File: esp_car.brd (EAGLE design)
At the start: 81.6 x 84 mm, 50 parts, among them IC1 TB6612FNG, IC2 LT1963ES8-3.3, SW2 SK-12D01, U1 ESP-WROOM-32_NOFLASH

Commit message: art work
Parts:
- removed IC1: TB6612FNG, adafruit:SSOP24
- added U$1: TB6612_NEW, adafruit_my:SSOP24_TB6612
- moved T0 49.4 mm to (76.8, 53.4)
- moved T2 42.5 mm to (57.1, 39.4)
- moved T1 36.7 mm to (68.2, 39.4)
- moved T3 33.0 mm to (47.8, 39.5)
- moved T5 32.1 mm to (18.0, 39.4)
- moved SJ1 2.80 mm to (36.6, 29.8), turned to 180 degrees
- moved C9 2.24 mm to (40.0, 70.0)
- moved SW2 2.00 mm to (40.0, 2.70)
- moved R2 1.03 mm to (38.1, 67.0)
- turned C10 to 180 degrees
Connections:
- net +3V3: now also U$1.20; no longer IC1.20
- net GND: now also U$1.0304, U$1.0910, U$1.18; no longer IC1.10, IC1.18, IC1.3, IC1.4, IC1.9
- net ML+: now also U$1.0102; no longer IC1.1, IC1.2
- net ML-: now also U$1.0506; no longer IC1.5, IC1.6
- net ML_IN1: now also U$1.21; no longer IC1.21
- net ML_IN2: now also U$1.22; no longer IC1.22
- net ML_PWM: now also U$1.23; no longer IC1.23
- net MR+: now also U$1.1112; no longer IC1.11, IC1.12
- net MR-: now also U$1.0708; no longer IC1.7, IC1.8
- net MR_IN1: now also U$1.17; no longer IC1.17
- net MR_IN2: now also U$1.16; no longer IC1.16
- net MR_PWM: now also U$1.15; no longer IC1.15
- net N$7: now also U$1.19; no longer IC1.19
- net VDD: now also U$1.1314, U$1.24; no longer IC1.13, IC1.14, IC1.24
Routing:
- net GND: track 0.00 -> 373.9 mm, vias 0 -> 12
- net +3V3: track 0.00 -> 226.4 mm, vias 0 -> 7
- net +5V: track 0.00 -> 196.2 mm, vias 0 -> 2
- net I2C_SDA: track 0.00 -> 141.2 mm
- net VCC: track 0.00 -> 124.2 mm, vias 0 -> 3
- net I2C_SCL: track 0.00 -> 123.5 mm, vias 0 -> 1
- net VDD: track 0.00 -> 112.5 mm, vias 0 -> 2
- net IO0: track 0.00 -> 109.4 mm, vias 0 -> 6
- net IO12: track 0.00 -> 76.6 mm
- net N$15: track 0.00 -> 65.3 mm, vias 0 -> 2
- net N$6: track 0.00 -> 61.8 mm
- net TX: track 0.00 -> 61.8 mm, vias 0 -> 3
- net N$18: track 0.00 -> 59.3 mm, vias 0 -> 2
- net N$9: track 0.00 -> 56.1 mm
- net RX: track 0.00 -> 51.1 mm, vias 0 -> 1
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
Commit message: ユニバーサル部分追加、NETCLASS調整
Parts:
- moved T0 9.43 mm to (70.0, 46.9)
- moved T1 2.96 mm to (69.8, 36.9)
- moved U$1 2.67 mm to (40.1, 58.3)
- moved C10 2.34 mm to (42.5, 66.2)
- moved R6 1.98 mm to (34.6, 56.0), turned to 90 degrees
- moved R2 1.37 mm to (37.0, 66.2)
- moved C9 0.81 mm to (39.4, 69.5)
- moved R5 0.46 mm to (32.6, 54.3)
- moved UNIV 0.29 mm to (62.2, 54.6)
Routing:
- net IO0: track 109.4 -> 71.2 mm, vias 6 -> 3
- net RX: track 51.1 -> 84.4 mm
- net IO12: track 76.6 -> 46.0 mm, vias 0 -> 2
- net TX: track 61.8 -> 34.4 mm, vias 3 -> 1
- net ML-: track 37.8 -> 12.1 mm, vias 3 -> 1
- net ENCR_B: track 41.3 -> 66.6 mm, vias 3 -> 1
- net +5V: track 196.2 -> 219.0 mm, vias 2 -> 5
- net MR-: track 35.4 -> 19.0 mm, vias 4 -> 1
- net I2C_SDA: track 141.2 -> 157.2 mm, vias 0 -> 4
- net N$19: track 31.9 -> 45.3 mm, vias 3 -> 2
- net N$6: track 61.8 -> 75.1 mm
- net DTR: track 12.6 -> 25.0 mm, vias 0 -> 1
- net +3V3: track 226.4 -> 235.6 mm, vias 7 -> 6
- net N$9: track 56.1 -> 65.3 mm
- net N$15: track 65.3 -> 73.5 mm, vias 2 -> 0
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
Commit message: 配線良し
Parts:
- moved R4 8.22 mm to (53.0, 69.5), turned to 0 degrees
- moved R3 4.43 mm to (51.0, 72.5), turned to 0 degrees
- moved C11 4.12 mm to (32.0, 75.5)
- moved R2 3.16 mm to (36.0, 69.2)
- moved C14 3.00 mm to (48.0, 76.0)
- moved LED_FL 1.12 mm to (22.0, 73.5)
- moved LED_FR 1.12 mm to (58.0, 73.5)
- moved C10 1.00 mm to (42.5, 67.2)
- moved C9 1.00 mm to (39.4, 68.5)
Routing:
- net IO0: track 71.2 -> 135.8 mm, vias 3 -> 2
- net RX: track 84.4 -> 38.9 mm, vias 1 -> 4
- net GND: track 376.5 -> 335.2 mm
- net I2C_SCL: track 128.6 -> 166.0 mm, vias 1 -> 5
- net +5V: track 219.0 -> 252.5 mm, vias 5 -> 11
- net ENCR_A: track 35.9 -> 64.8 mm, vias 2 -> 4
- net I2C_SDA: track 157.2 -> 132.8 mm, vias 4 -> 3
- net VDD: track 114.3 -> 92.5 mm, vias 4 -> 5
- net EN: track 32.5 -> 52.3 mm, vias 4 -> 3
- net IO12: track 46.0 -> 64.8 mm, vias 2 -> 6
- net N$6: track 75.1 -> 60.7 mm
- net MR_PWM: track 16.4 -> 30.6 mm
- net N$15: track 73.5 -> 60.2 mm
- net DTR: track 25.0 -> 13.4 mm, vias 1 -> 0
- net N$9: track 65.3 -> 56.0 mm
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
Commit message: wire 100% 初版
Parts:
- removed U1: ESP-WROOM-32_NOFLASH, esp32 _my:ESP-WROOM-32_NOFLASH
- added ESP32: ESP-WROOM-32_NOFLASH_PINHEAD, esp32 _my:ESP-WROOM-32_NOFLASH_PINHEAD
- moved C1 12.5 mm to (15.0, 62.2), turned to 90 degrees
- moved R2 4.15 mm to (39.8, 67.6)
- moved C9 3.53 mm to (39.0, 65.0), turned to 90 degrees
- moved EN(RESET) 2.54 mm to (15.0, 56.0)
- moved C10 2.42 mm to (43.3, 65.0), turned to 90 degrees
- moved C6 1.78 mm to (27.5, 62.2)
- moved SJ1 1.70 mm to (34.9, 29.7)
- moved C8 1.45 mm to (29.4, 28.8)
- moved R6 1.44 mm to (33.4, 56.8)
- moved R5 0.90 mm to (33.4, 53.8)
- moved C5 0.51 mm to (27.5, 58.5)
- moved U$1 0.13 mm to (40.0, 58.3)
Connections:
- net +3V3: now also ESP32.P$2; no longer U1.2
- net EN: now also ESP32.P$3; no longer U1.3
- net ENCL_A: now also ESP32.P$6; no longer U1.6
- net ENCL_B: now also ESP32.P$7; no longer U1.7
- net ENCR_A: now also ESP32.P$4; no longer U1.4
- net ENCR_B: now also ESP32.P$5; no longer U1.5
- net GND: now also ESP32.P$1, ESP32.P$15, ESP32.P$38; no longer U1.1, U1.15, U1.38
- net I2C_SCL: now also ESP32.P$36; no longer U1.36
- net I2C_SDA: now also ESP32.P$33; no longer U1.33
- net IO0: now also ESP32.P$25; no longer U1.25
- net IO12: now also ESP32.P$14; no longer U1.14
- net IO15: now also ESP32.P$23; no longer U1.23
- net IO2: now also ESP32.P$24; no longer U1.24
- net IO27: now also ESP32.P$12; no longer U1.12
- net IO4: now also ESP32.P$26; no longer U1.26
- net IO5: now also ESP32.P$29; no longer U1.29
- net ML_IN1: now also ESP32.P$27; no longer U1.27
- net ML_IN2: now also ESP32.P$28; no longer U1.28
- net ML_PWM: now also ESP32.P$11; no longer U1.11
- net MR_IN1: now also ESP32.P$30; no longer U1.30
- net MR_IN2: now also ESP32.P$31; no longer U1.31
- net MR_PWM: now also ESP32.P$10; no longer U1.10
- net N$18: now also ESP32.P$16; no longer U1.16
- net N$19: now also ESP32.P$9; no longer U1.9
- net N$3: now also ESP32.P$8; no longer U1.8
- net N$5: now also ESP32.P$37; no longer U1.37
- net N$8: now also ESP32.P$13; no longer U1.13
- net RX: now also ESP32.P$34; no longer U1.34
- net TX: now also ESP32.P$35; no longer U1.35
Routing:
- net IO0: track 135.8 -> 82.8 mm, vias 2 -> 4
- net +5V: track 252.5 -> 209.7 mm, vias 11 -> 6
- net ENCR_A: track 64.8 -> 34.2 mm, vias 4 -> 0
- net ENCR_B: track 65.8 -> 41.5 mm, vias 3 -> 2
- net EN: track 52.3 -> 29.9 mm, vias 3 -> 0
- net GND: track 335.2 -> 357.0 mm
- net MR_PWM: track 30.6 -> 14.4 mm, vias 2 -> 1
- net +3V3: track 238.8 -> 226.0 mm, vias 3 -> 7
- net N$19: track 36.0 -> 28.2 mm, vias 5 -> 2
- net ENCL_B: track 24.5 -> 16.7 mm, vias 1 -> 0
- net N$6: track 60.7 -> 66.5 mm, vias 0 -> 2
- net N$7: track 11.3 -> 17.0 mm, vias 0 -> 2
- net IO15: track 30.7 -> 25.2 mm
- net IO2: track 28.1 -> 33.0 mm, vias 2 -> 0
- net VCC: track 124.3 -> 128.8 mm, vias 4 -> 3
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
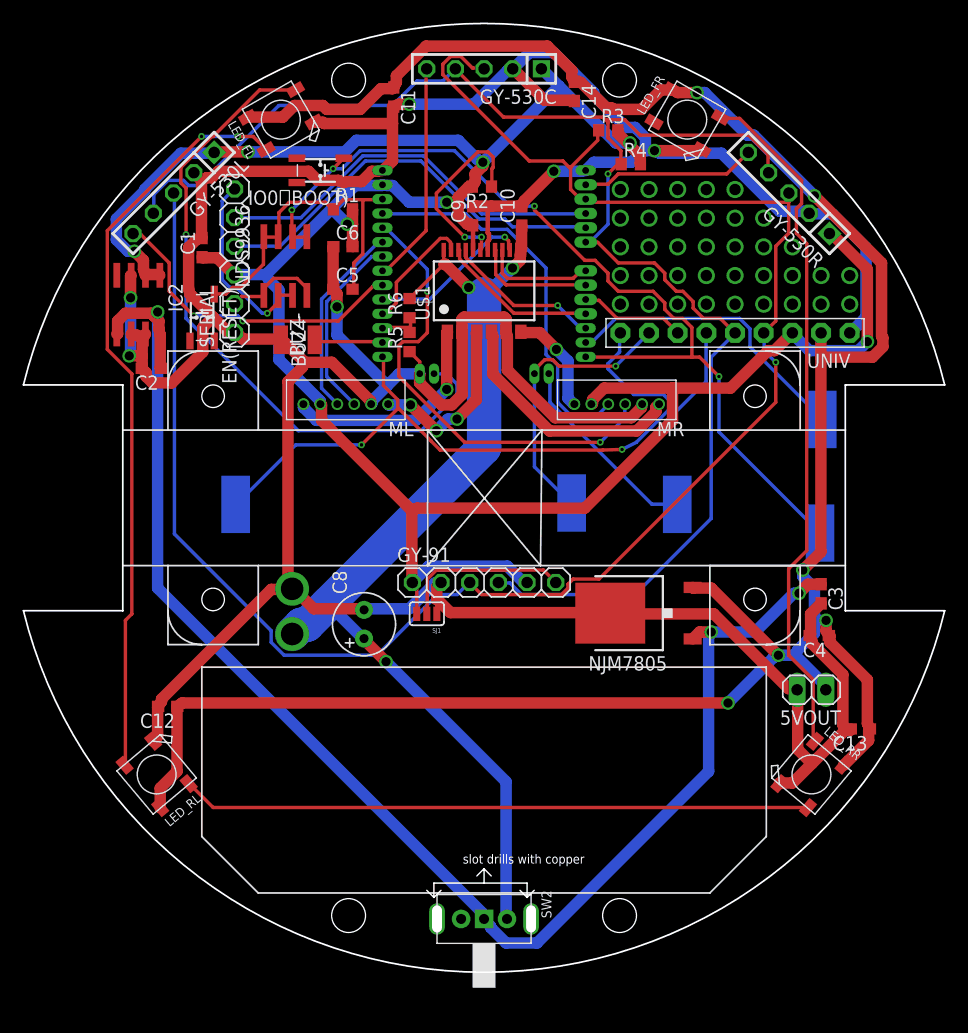
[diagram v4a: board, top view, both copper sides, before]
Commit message: 5vレギュレータをLDOに変更、配線100%　v2
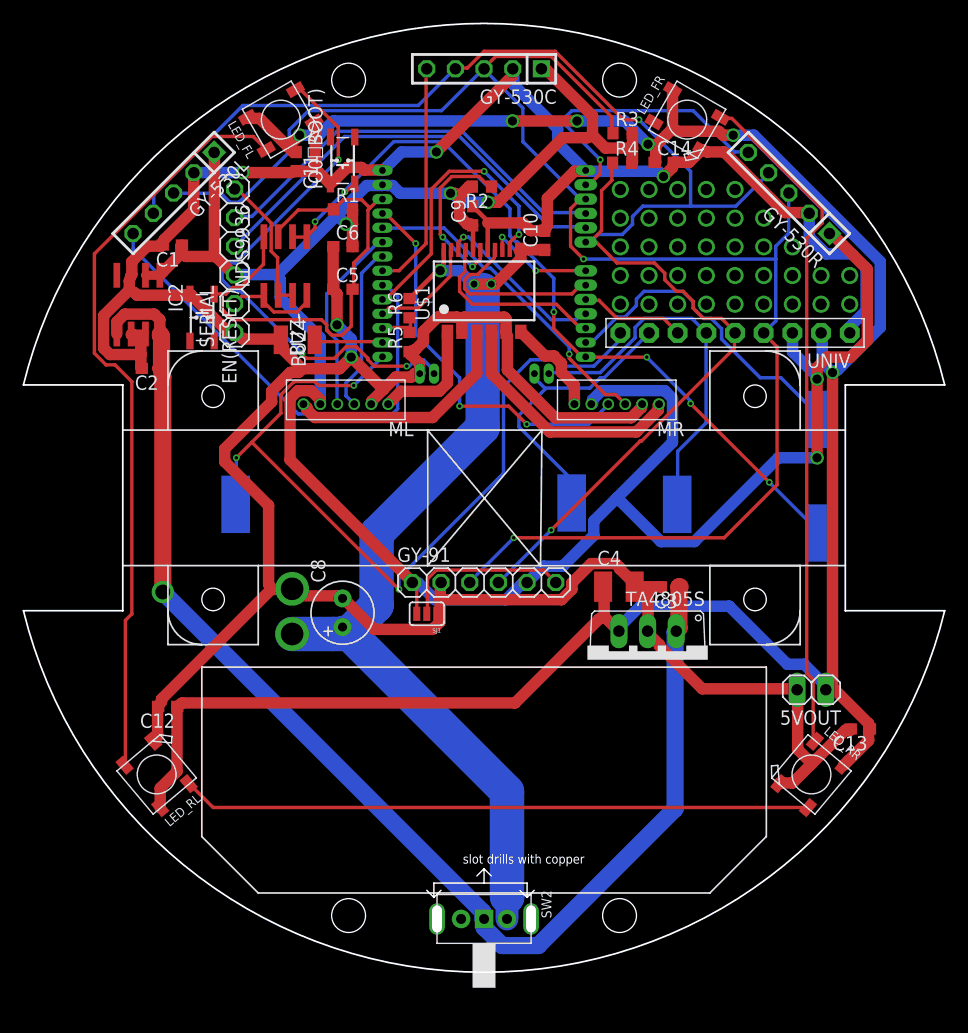
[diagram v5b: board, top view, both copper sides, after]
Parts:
- removed NJM7805: 7806DT, linear:TO252
- added TA4805S: 788TV, linear:TO220V
- C3: value 10uF -> 0.33u
- C4: value 10uF -> 33u; device rcl:C1608 -> rcl:C3225
- moved C4 18.3 mm to (51.9, 32.1), turned to 0 degrees
- moved C3 13.4 mm to (56.5, 32.1), turned to 180 degrees
- moved C11 10.4 mm to (23.4, 69.8)
- moved C14 10.1 mm to (56.0, 69.7), turned to 0 degrees
- moved C10 2.96 mm to (45.4, 62.8)
- moved C1 2.65 mm to (12.4, 62.4), turned to 180 degrees
- moved C8 2.16 mm to (27.5, 29.8)
- moved IO0（BOOT) 2.16 mm to (27.5, 69.9), turned to 90 degrees
- moved R3 1.30 mm to (52.3, 72.3)
- moved R4 0.77 mm to (52.2, 69.7)
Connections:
- removed net ML+: ML.1, U$1.0102
- new net N$38: ML.1, U$1.0506
- net +5V: now also TA4805S.3; no longer NJM7805.2
- net GND: now also TA4805S.2; no longer NJM7805.3
- net ML-: now also U$1.0102; no longer U$1.0506
- net VCC: now also TA4805S.1; no longer NJM7805.1
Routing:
- net GND: track 357.0 -> 329.2 mm, vias 6 -> 5
- net N$38: track 0.00 -> 21.2 mm
- net ML+: track 19.7 -> 0.00 mm, vias 1 -> 0
- net I2C_SCL: track 164.9 -> 146.7 mm, vias 1 -> 2
- net EN: track 29.9 -> 45.0 mm
- net VCC: track 128.8 -> 113.9 mm, vias 3 -> 1
- net N$19: track 28.2 -> 42.7 mm, vias 2 -> 0
- net IO12: track 61.0 -> 75.4 mm, vias 2 -> 3
- net ENCR_B: track 41.5 -> 28.6 mm, vias 2 -> 1
- net IO0: track 82.8 -> 70.3 mm, vias 4 -> 6
- net N$18: track 59.3 -> 47.1 mm, vias 1 -> 3
- net MR_PWM: track 14.4 -> 25.7 mm, vias 1 -> 2
- net N$5: track 15.6 -> 25.9 mm, vias 0 -> 1
- net +5V: track 209.7 -> 202.0 mm
- net +3V3: track 226.0 -> 219.3 mm, vias 7 -> 5
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
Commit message: 電源用MOSFET追加、VDD見直し
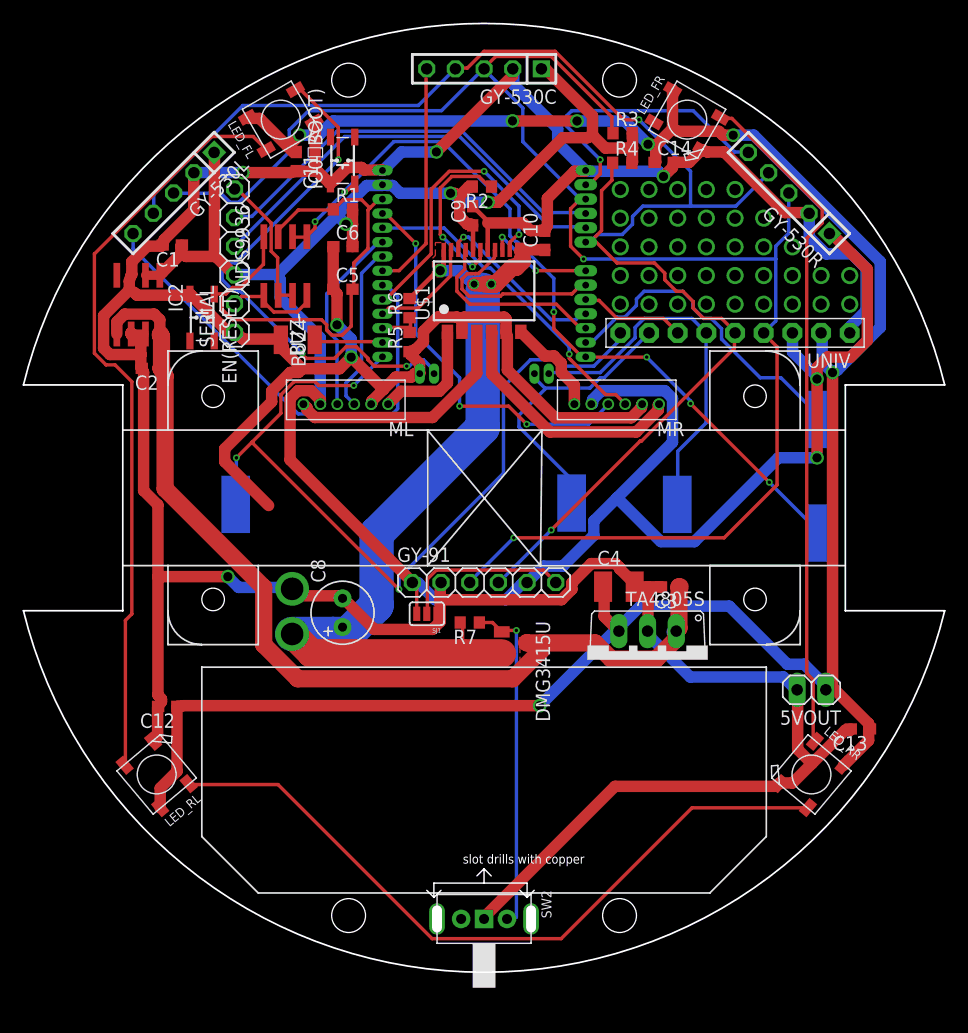
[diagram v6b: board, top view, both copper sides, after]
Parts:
- added DMG3415U: BSS84, transistor-small-signal:SOT23
- added R7: 100k, rcl:R0603
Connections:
- new net N$39: DMG3415U.1, R7.1, SW2.A
- net GND: now also SW2.COM
- net VCC: now also DMG3415U.3; no longer SW2.COM
- net VDD: now also DMG3415U.2, R7.2; no longer SW2.A
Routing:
- net GND: track 329.2 -> 380.5 mm, vias 5 -> 6
- net N$39: track 0.00 -> 30.1 mm, vias 0 -> 1
- net VCC: track 113.9 -> 85.3 mm, vias 1 -> 0
- net N$9: track 55.7 -> 65.6 mm
- net VDD: track 91.7 -> 83.9 mm
- net +5V: track 202.0 -> 202.8 mm, vias 6 -> 7
- net MR_IN1: track 16.2 -> 16.9 mm
- added copper zone on layer 1, net VCC
- added copper zone on layer 1, net VDD

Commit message: airwireなし
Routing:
- net VDD: track 83.9 -> 84.7 mm
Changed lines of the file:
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@@
 <wire x1="43.246" y1="61.9724" x2="45.3626" y2="61.9724" width="1.016" layer="1"/>
 <wire x1="45.3626" y1="61.9724" x2="45.378" y2="61.957" width="1.016" layer="1"/>
-<wire x1="43.246" y1="61.17005625" x2="43.246" y2="61.9724" width="1.016" layer="1"/>
+<wire x1="43.246" y1="61.9724" x2="43.246" y2="61.17005625" width="1.016" layer="1"/>
 <wire x1="37.8333" y1="60.1218" x2="36.1188" y2="60.1218" width="1.016" layer="16"/>
 <wire x1="38.6334" y1="59.3217" x2="37.8333" y2="60.1218" width="1.016" layer="16"/>
@@
 <vertex x="36.576" y="62.611"/>
 </polygon>
-<wire x1="43.3894" y1="61.17005625" x2="43.246" y2="61.17005625" width="0" layer="19" extent="1-1"/>
-<wire x1="39.116" y1="58.928" x2="39.116" y2="58.9153" width="0" layer="19" extent="1-1"/>
+<wire x1="39.116" y1="58.928" x2="39.1287" y2="58.9153" width="0.1524" layer="1"/>
+<wire x1="39.1287" y1="58.9153" x2="39.6180875" y2="58.9153" width="0.1524" layer="1"/>
+<wire x1="43.246" y1="61.17005625" x2="43.246" y2="61.09764375" width="0.1524" layer="1"/>
+<wire x1="43.246" y1="61.09764375" x2="43.3894" y2="60.95424375" width="0.1524" layer="1"/>
 </signal>
 <signal name="+3V3" class="1">
